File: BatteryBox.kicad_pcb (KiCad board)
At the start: 2 copper layers, 100 x 100 mm, 33 parts, among them J1 Conn_01x02, J10 Conn_01x02, J11 Conn_01x02, J12 Conn_01x02, J13 Conn_01x02, J14 Conn_01x02, J15 Conn_01x02, J2 Conn_01x02, J3 Conn_01x02, J4 Conn_01x04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

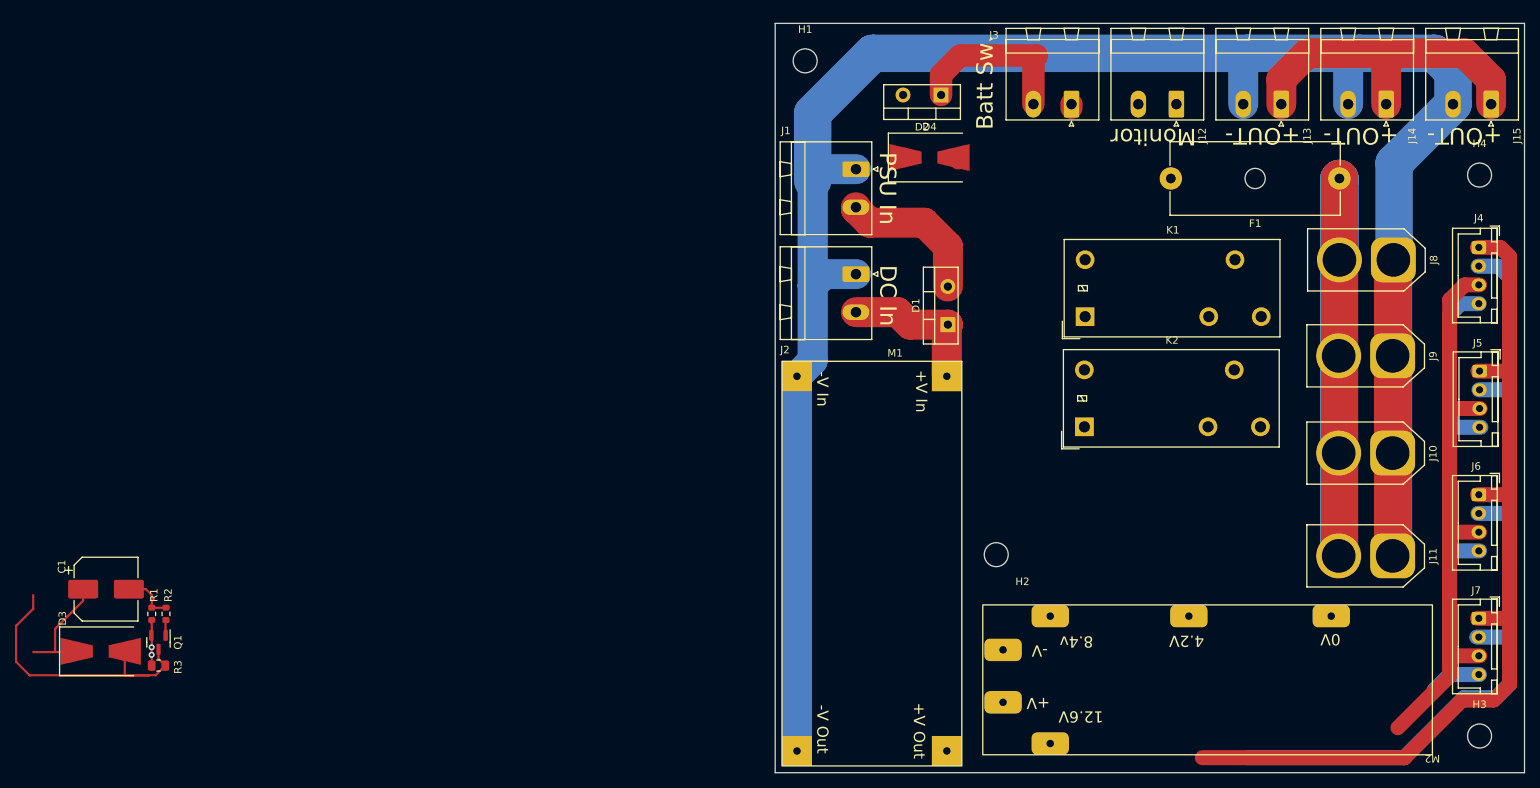
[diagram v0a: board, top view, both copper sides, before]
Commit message: Finalising PCB layout. Needs final component puchase and footprint check.
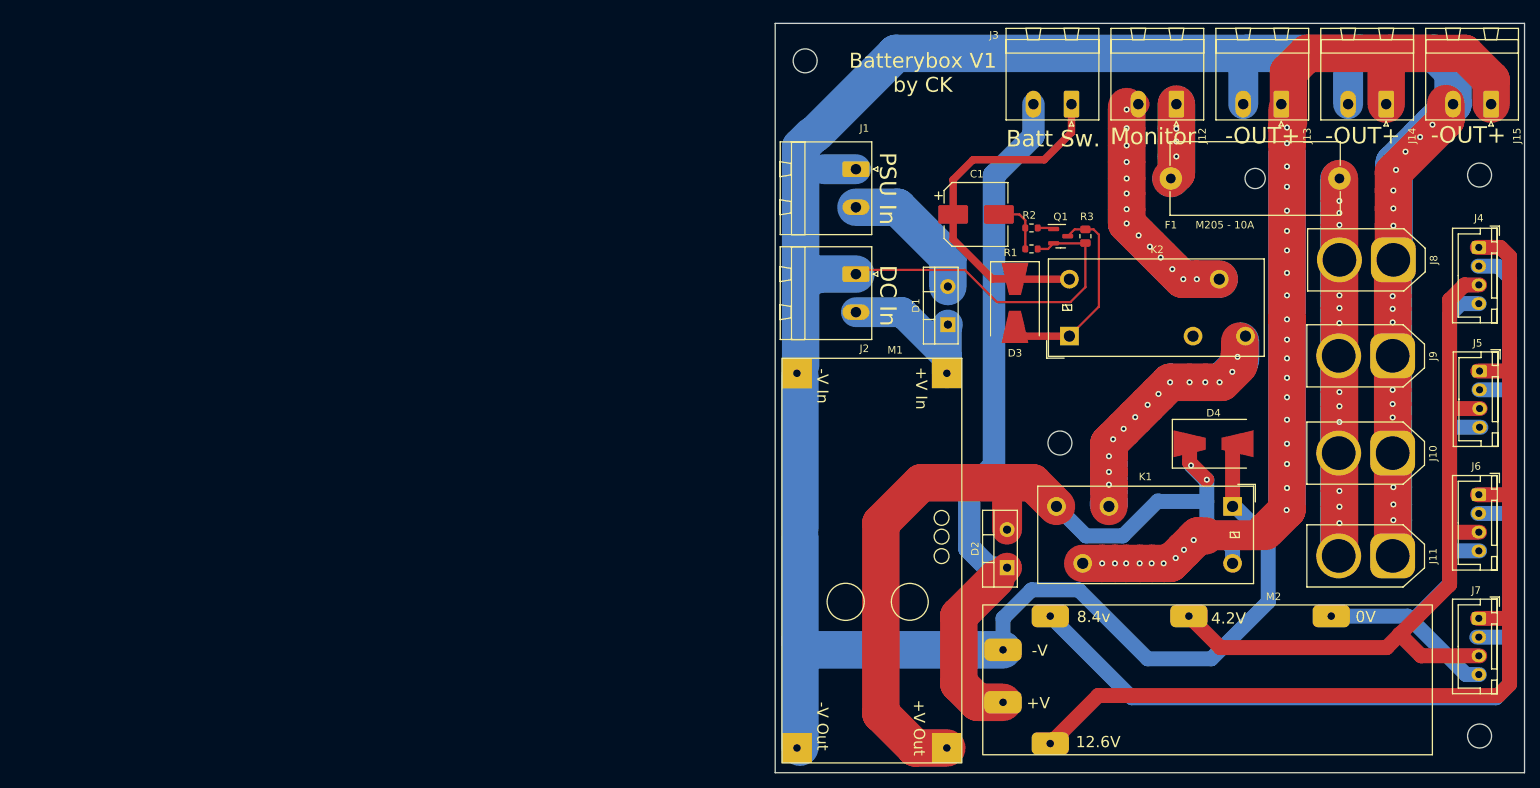
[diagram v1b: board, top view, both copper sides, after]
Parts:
- F1: value 10A -> M205 - 10A
- moved R3 136.3 mm to (100.4, 87.4), turned to -90 degrees
- moved Q1 132.0 mm to (97.1, 87.4), turned to 0 degrees
- moved D3 130.6 mm to (91.0, 96.3), turned to -90 degrees
- moved R1 127.1 mm to (93.2, 89.1), turned to 180 degrees
- moved R2 126.5 mm to (93.2, 86.3), turned to 0 degrees
- moved C1 126.4 mm to (85.8, 84.5)
- moved D2 63.7 mm to (89.9, 131.6), turned to 90 degrees
- moved D4 53.8 mm to (117.5, 115.1)
- moved K1 32.1 mm to (120.0, 123.5), turned to 180 degrees
- moved H2 17.2 mm to (97.0, 115.0)
- moved K2 12.3 mm to (98.3, 100.7)
- moved M1 0.40 mm to (83.9, 103.7)
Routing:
- net Net-(J15-Pad1): track 44.4 -> 199.9 mm, vias 0 -> 28
- net GND: track 316.1 -> 470.7 mm, vias 2 -> 16
- net Net-(D2-Pad2): track 0.00 -> 114.4 mm, vias 0 -> 2
- net Net-(D2-Pad1): track 23.2 -> 94.0 mm
- net Net-(K1-Pad2): track 0.00 -> 64.3 mm, vias 0 -> 14
- net Net-(J12-Pad2): track 0.00 -> 63.5 mm, vias 0 -> 14
- net Net-(C1-Pad1): track 16.3 -> 47.9 mm
- net Net-(J4-Pad2): track 108.7 -> 136.2 mm
- net Net-(J4-Pad3): track 74.5 -> 101.3 mm
- net Net-(F1-Pad2): track 0.00 -> 20.5 mm, vias 0 -> 3
- net Net-(J4-Pad1): track 118.0 -> 137.5 mm
- net Net-(D3-Pad2): track 40.0 -> 27.8 mm
- net Net-(F1-Pad1): track 112.0 -> 100.8 mm, vias 0 -> 12
- net Net-(J4-Pad4): track 66.7 -> 76.5 mm
- net Net-(D1-Pad1): track 19.9 -> 21.2 mm
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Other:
- board text added: "-OUT+"
- board text added: "Batterybox V1 by CK"
- board text removed: "+OUT-"
